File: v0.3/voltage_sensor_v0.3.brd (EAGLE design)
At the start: 77 x 105 mm, 59 parts, among them IC1 AP2112K-3.3TRG1, J2 236-404_000-009_999-950, J3 MC000048, J9 RJ11-6, T1 ZMPT101B, T2 ZMPT101B, T3 ZMPT101B

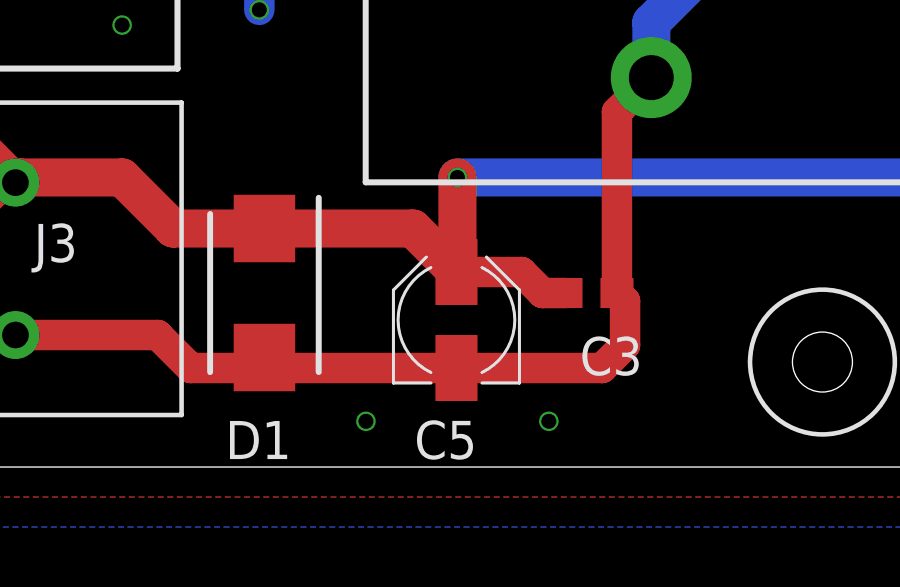
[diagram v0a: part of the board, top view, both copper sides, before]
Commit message: increase footprint of C5
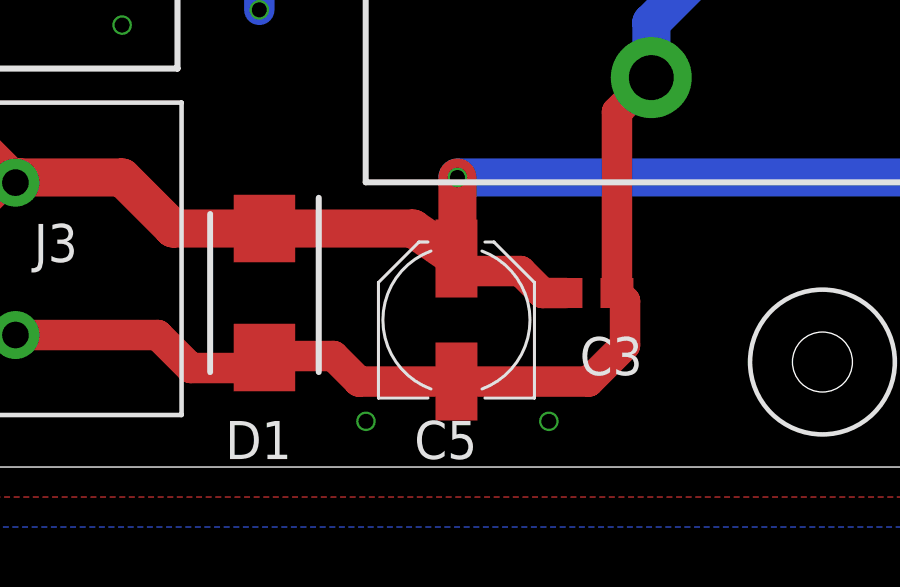
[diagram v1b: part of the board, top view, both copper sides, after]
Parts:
- C5: device rcl:PANASONIC_B -> rcl:PANASONIC_C
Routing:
- net GND: track 205.9 -> 206.6 mm
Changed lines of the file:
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@@
 <setting verticaltext="up"/>
 </settings>
-<grid distance="20" unitdist="mil" unit="mil" style="lines" multiple="1" display="yes" altdistance="5" altunitdist="mil" altunit="mil"/>
+<grid distance="3.93700787" unitdist="mil" unit="mil" style="lines" multiple="1" display="yes" altdistance="5" altunitdist="mil" altunit="mil"/>
 <layers>
 <layer number="1" name="Top" color="4" fill="1" visible="yes" active="yes"/>
@@
 <attribute name="VALUE" x="56.411" y="3.768" size="1.27" layer="27"/>
 </element>
-<element name="C5" library="rcl" library_urn="urn:adsk.eagle:library:334" package="PANASONIC_B" package3d_urn="urn:adsk.eagle:package:23421/2" value="180uF" x="52.8" y="4.9" smashed="yes" rot="R90">
+<element name="C5" library="rcl" library_urn="urn:adsk.eagle:library:334" package="PANASONIC_C" package3d_urn="urn:adsk.eagle:package:23422/2" value="180uF" x="52.8" y="4.9" smashed="yes" rot="R90">
 <attribute name="NAME" x="53.489" y="1.538" size="1.27" layer="25" font="vector" ratio="20" rot="R180"/>
 <attribute name="POPULARITY" value="4" x="52.8" y="4.9" size="1.778" layer="27" rot="R90" display="off"/>
@@
 <wire x1="58.15" y1="5.8" x2="58.15" y2="11.835" width="1.016" layer="1"/>
 <wire x1="58.15" y1="11.835" x2="59.295" y2="12.98" width="1.016" layer="1"/>
-<wire x1="52.8" y1="3.3" x2="46.75" y2="3.3" width="1.016" layer="1"/>
 <wire x1="46.75" y1="3.3" x2="46.4" y2="3.65" width="1.016" layer="1"/>
-<wire x1="52.8" y1="3.3" x2="57.656" y2="3.3" width="1.016" layer="1"/>
-<wire x1="57.656" y1="3.3" x2="58.42" y2="4.064" width="1.016" layer="1"/>
-<wire x1="58.42" y1="4.064" x2="58.42" y2="5.53" width="1.016" layer="1"/>
+<wire x1="58.42" y1="5.53" x2="58.42" y2="4.064" width="1.016" layer="1"/>
 <wire x1="58.42" y1="5.53" x2="58.15" y2="5.8" width="1.016" layer="1"/>
 <wire x1="38.1" y1="4.4" x2="42.844" y2="4.4" width="1.016" layer="1"/>
@@
 <via x="36.068" y="24.384" extent="1-16" drill="0.5"/>
 <via x="41.656" y="14.732" extent="1-16" drill="0.5"/>
+<wire x1="52.8" y1="2.85" x2="49.55" y2="2.85" width="1.016" layer="1"/>
+<wire x1="49.55" y1="2.85" x2="48.7" y2="3.7" width="1.016" layer="1"/>
+<wire x1="48.7" y1="3.7" x2="47.15" y2="3.7" width="1.016" layer="1"/>
+<wire x1="47.15" y1="3.7" x2="46.75" y2="3.3" width="1.016" layer="1"/>
+<wire x1="57.206" y1="2.85" x2="52.8" y2="2.85" width="1.016" layer="1"/>
+<wire x1="58.42" y1="4.064" x2="57.206" y2="2.85" width="1.016" layer="1"/>
+<wire x1="3.048" y1="90.424" x2="14.224" y2="102.108" width="0" layer="19" extent="1-1"/>
+<wire x1="2.706" y1="80.28" x2="3.048" y2="90.424" width="0" layer="19" extent="1-1"/>
+<wire x1="13.716" y1="1.524" x2="15.15" y2="3.65" width="0" layer="19" extent="1-1"/>
+<wire x1="49.784" y1="1.524" x2="52.8" y2="2.85" width="0" layer="19" extent="1-1"/>
+<wire x1="55.88" y1="1.524" x2="52.8" y2="2.85" width="0" layer="19" extent="1-1"/>
+<wire x1="24.22" y1="9.31" x2="21.75" y2="6" width="0" layer="19" extent="1-1"/>
+<wire x1="11.176" y1="8.636" x2="12" y2="3.65" width="0" layer="19" extent="1-1"/>
+<wire x1="41.656" y1="14.732" x2="38.1" y2="4.4" width="0" layer="19" extent="1-1"/>
+<wire x1="46.228" y1="15.24" x2="41.656" y2="14.732" width="0" layer="19" extent="1-1"/>
+<wire x1="36.068" y1="24.384" x2="37.592" y2="25.908" width="0" layer="19" extent="1-1"/>
+<wire x1="14.224" y1="61.468" x2="2.706" y2="61.484" width="0" layer="19" extent="1-1"/>
+<wire x1="14.224" y1="79.756" x2="2.706" y2="80.28" width="0" layer="19" extent="1-1"/>
+<wire x1="15.748" y1="42.164" x2="2.706" y2="42.18" width="0" layer="19" extent="1-1"/>
+<wire x1="6.096" y1="21.844" x2="11.176" y2="8.636" width="0" layer="19" extent="1-1"/>
 </signal>
 <signal name="N$25">
@@
 <wire x1="70.612" y1="36.292" x2="73.32" y2="39" width="1.27" layer="1"/>
 <wire x1="70.612" y1="14.368" x2="70.612" y2="36.292" width="1.27" layer="1"/>
-<wire x1="52.8" y1="6.5" x2="54.968" y2="6.5" width="1.016" layer="1"/>
-<wire x1="55.668" y1="5.8" x2="56.45" y2="5.8" width="1.016" layer="1"/>
-<wire x1="54.968" y1="6.5" x2="55.668" y2="5.8" width="1.016" layer="1"/>
+<wire x1="56.45" y1="5.8" x2="55.668" y2="5.8" width="1.016" layer="1"/>
 <wire x1="46.4" y1="7.95" x2="46.064" y2="8.286" width="1.016" layer="1"/>
 <wire x1="21.75" y1="6.95" x2="32.512" y2="6.95" width="0.508" layer="1"/>
@@
 <wire x1="29.626" y1="4.064" x2="32.512" y2="6.95" width="0.508" layer="1"/>
 <wire x1="24.892" y1="4.064" x2="29.626" y2="4.064" width="0.508" layer="1"/>
-<wire x1="52.8" y1="6.5" x2="52.832" y2="6.532" width="1.27" layer="1"/>
+<wire x1="52.8" y1="6.95" x2="52.832" y2="6.532" width="1.27" layer="1"/>
 <wire x1="52.832" y1="6.532" x2="52.832" y2="9.652" width="1.27" layer="1"/>
 <via x="52.832" y="9.652" extent="1-16" drill="0.5"/>
@@
 <wire x1="68.672" y1="9.652" x2="72" y2="12.98" width="1.27" layer="16"/>
 <wire x1="46.4" y1="7.95" x2="51.35" y2="7.95" width="1.27" layer="1"/>
-<wire x1="51.35" y1="7.95" x2="52.8" y2="6.5" width="1.27" layer="1"/>
+<wire x1="51.35" y1="7.95" x2="52.8" y2="6.95" width="1.27" layer="1"/>
 <wire x1="38.1" y1="9.48" x2="36.576" y2="11.004" width="1.27" layer="1"/>
 <wire x1="38.809" y1="22.045" x2="39.438" y2="22.045" width="1.27" layer="1"/>
@@
 <wire x1="41.656" y1="9.652" x2="38.272" y2="9.652" width="1.27" layer="1"/>
 <wire x1="38.272" y1="9.652" x2="38.1" y2="9.48" width="1.27" layer="1"/>
+<wire x1="54.936" y1="6.532" x2="52.832" y2="6.532" width="1.016" layer="1"/>
+<wire x1="55.668" y1="5.8" x2="54.936" y2="6.532" width="1.016" layer="1"/>
 </signal>
 <signal name="N$17">

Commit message: v0.3 changes
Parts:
- removed J3: MC000048, 5mm-terminal:CONN2_00048_MTC
- added J1: 1017505, 1017505:1017505
- J2: value 236-404_000-009_999-950 -> 20020316-H021B01LF; device 236-404_000-009_999-950:236404000009999950 -> 20020316-H021B01LF:20020316H021B01LF
- moved J2 96.6 mm to (36.6, 4.21), turned to 90 degrees
- moved R34 25.1 mm to (73.2, 55.5), turned to 270 degrees
- moved F3 9.06 mm to (45.8, 74.6)
- moved F2 9.01 mm to (50.9, 74.6)
- moved F1 9.00 mm to (56.0, 74.6)
- moved R31 7.83 mm to (63.9, 63.6), turned to 270 degrees
- moved R32 5.00 mm to (58.9, 58.8)
- moved R19 4.71 mm to (42.0, 63.2), turned to 0 degrees
- moved R33 2.00 mm to (53.4, 54.0)
- moved U$3 0.92 mm to (72.3, 92.9)
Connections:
- net 5V: now also J2.2; no longer J3.2
- net GND: now also J2.1; no longer J3.1
- net L1: now also R31.1
- net N$16: now also J1.7, J1.8; no longer J2.7, J2.8
- net N$17: no longer R31.2
- net N$7: now also J1.3, J1.4; no longer J2.3, J2.4
- net N$8: now also J1.5, J1.6; no longer J2.5, J2.6
- net NEUTRAL: now also J1.1, J1.2, R31.2; no longer J2.1, J2.2, R31.1
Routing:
- net NEUTRAL: track 186.8 -> 146.1 mm
- net N$17: track 66.3 -> 31.2 mm
- net L1: track 44.6 -> 57.1 mm, vias 0 -> 1
- net L3: track 40.7 -> 50.4 mm, vias 0 -> 2
- net GND: track 206.6 -> 198.5 mm
- net N$7: track 16.8 -> 14.2 mm
- net N$16: track 16.6 -> 14.3 mm
- net N$8: track 16.4 -> 14.2 mm
- net L2: track 25.6 -> 24.4 mm
- net N$14: track 3.82 -> 2.91 mm
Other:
- outline, holes or cut-outs redrawn
- board text added: "a"
- board text added: "c"
